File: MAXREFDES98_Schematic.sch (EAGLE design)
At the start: 34 parts, among them U1 MB110S-TP, U2 MB110S-TP, U3 MAX5969AETB+

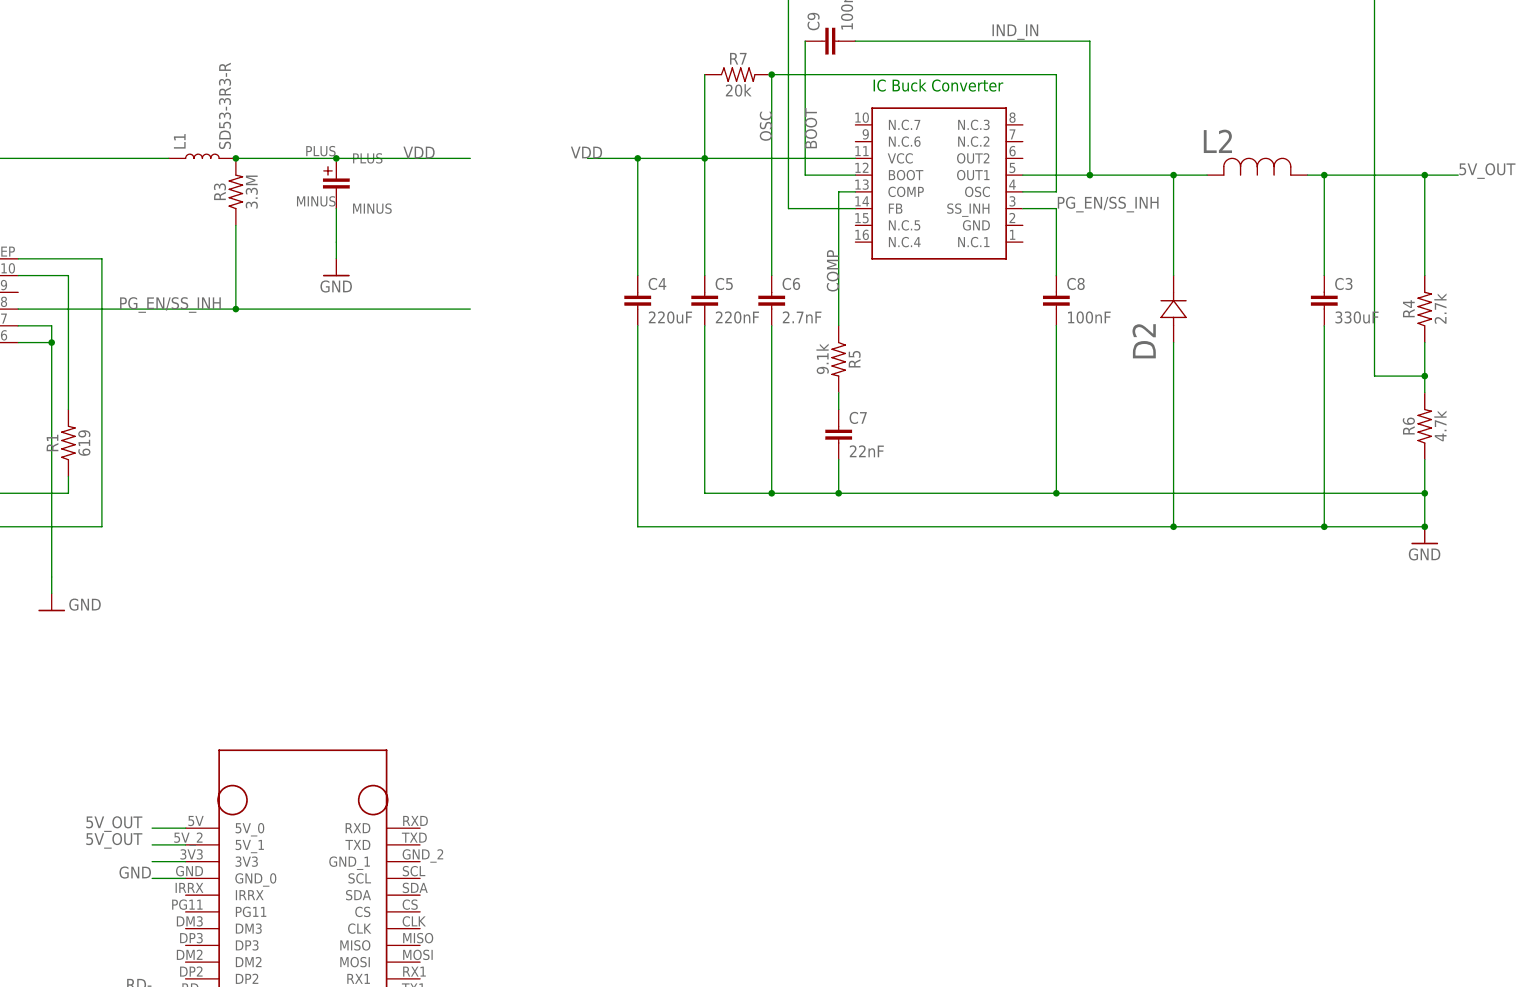
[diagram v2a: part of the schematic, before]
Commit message: Schematic fixes, parts update, replace parts on board
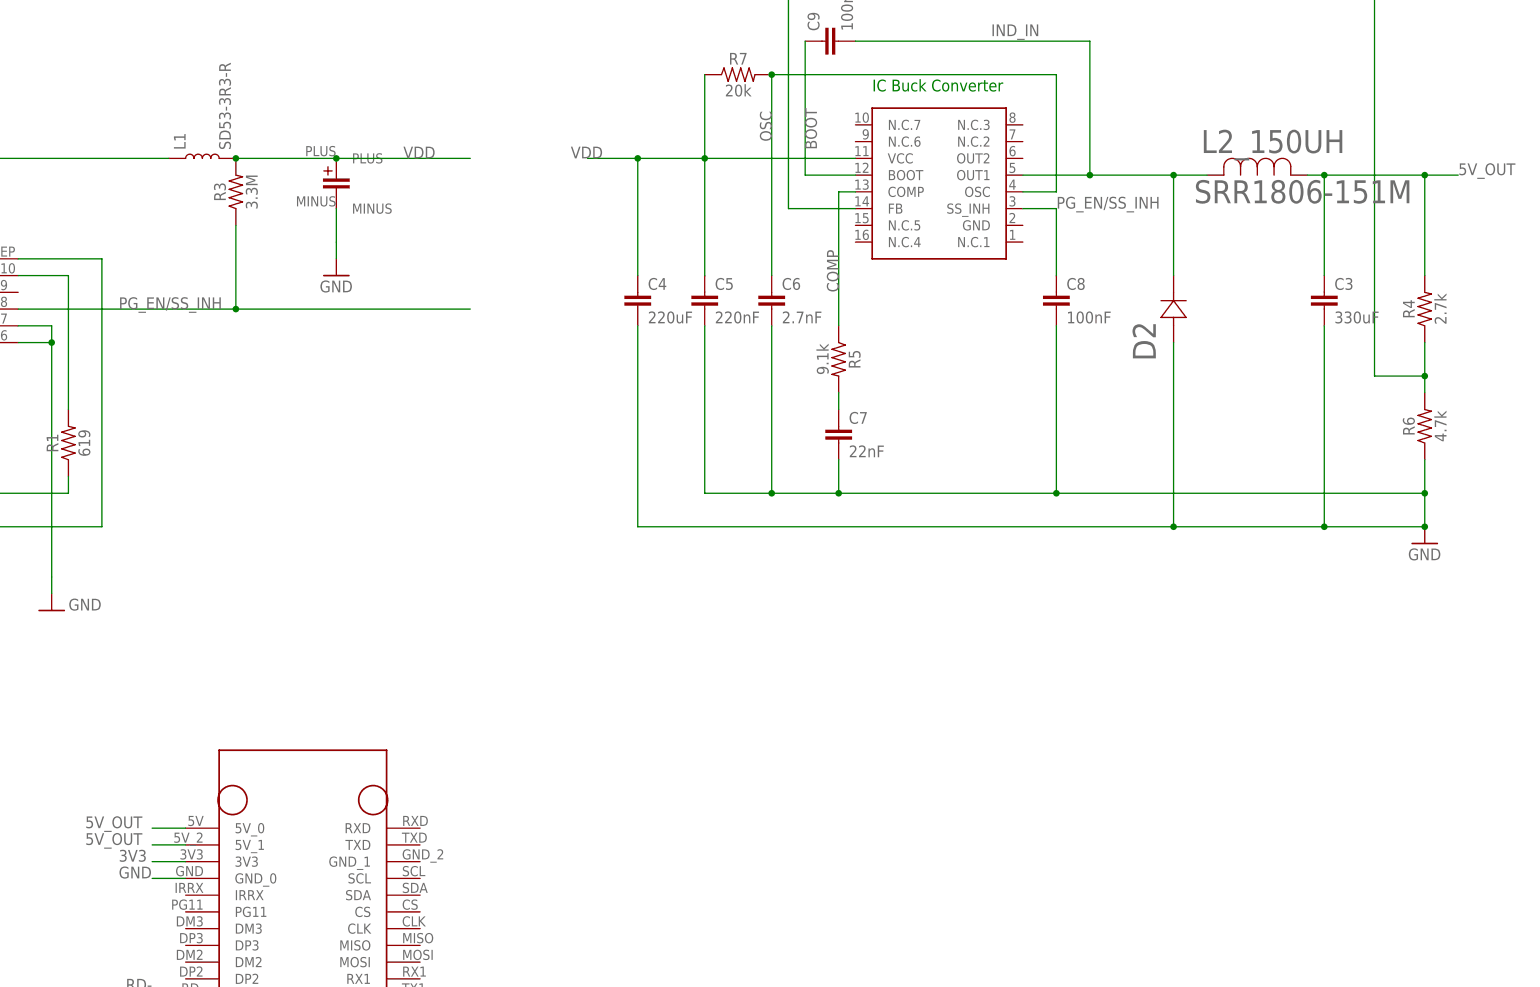
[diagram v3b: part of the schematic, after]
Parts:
- removed L2: SRR1806-151M, Camera_Board_Parts_09_30_2020:SRR1806-151M
- added L2_150UH: SRR1806-151M, CameraBoard_Library:SRR1806-151M
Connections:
- net N$8 renamed 3V3
- net 5V_OUT: now also L2_150UH.1; no longer L2.1
- net IND_IN: now also L2_150UH.2; no longer L2.2
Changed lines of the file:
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@@
 <part name="FRAME1" library="frames" library_urn="urn:adsk.eagle:library:229" deviceset="FRAME_B_L" device=""/>
 <part name="CONN" library="Camera_Board_Parts_09_30_2020" deviceset="TERM_BLOCK_PLUG_8POS_STR_2.5MM" device="" package3d_urn="urn:adsk.eagle:package:24353855/2"/>
-<part name="U$2" library="Camera_Board_Parts_09_30_2020" deviceset="NANO_PI" device=""/>
+<part name="U$2" library="Camera_Board_Parts_09_30_2020" deviceset="NANO_PI" device="" package3d_urn="urn:adsk.eagle:package:24353856/1"/>
 <part name="R10" library="SparkFun-Resistors" library_urn="urn:adsk.eagle:library:532" deviceset="0OHM" device="-0603-1/10W-5%" package3d_urn="urn:adsk.eagle:package:39650/1" value="0"/>
 <part name="R8" library="SparkFun-Resistors" library_urn="urn:adsk.eagle:library:532" deviceset="0OHM" device="-0603-1/10W-5%" package3d_urn="urn:adsk.eagle:package:39650/1" value="0"/>
@@
 <part name="GND9" library="supply1" library_urn="urn:adsk.eagle:library:371" deviceset="GND" device=""/>
 <part name="GND14" library="supply1" library_urn="urn:adsk.eagle:library:371" deviceset="GND" device=""/>
-<part name="U$1" library="Camera_Board_Parts_09_30_2020" deviceset="L4978D013TR" device=""/>
+<part name="U$1" library="Camera_Board_Parts_09_30_2020" deviceset="L4978D013TR" device="" package3d_urn="urn:adsk.eagle:package:24353853/1"/>
 <part name="C3" library="SparkFun-Capacitors" library_urn="urn:adsk.eagle:library:510" deviceset="4.7UF" device="0603" package3d_urn="urn:adsk.eagle:package:37414/1" value="330uF"/>
 <part name="C4" library="SparkFun-Capacitors" library_urn="urn:adsk.eagle:library:510" deviceset="4.7UF" device="0603" package3d_urn="urn:adsk.eagle:package:37414/1" value="220uF"/>
@@
 <part name="R7" library="SparkFun-Resistors" library_urn="urn:adsk.eagle:library:532" deviceset="0.22OHM" device="-0805-1/4W-1%" package3d_urn="urn:adsk.eagle:package:39651/1" value="20k"/>
 <part name="D2" library="Camera_Board_Parts_09_30_2020" deviceset="STPS3L60U" device="SMB_STM-M"/>
-<part name="L2" library="Camera_Board_Parts_09_30_2020" deviceset="SRR1806-151M" device=""/>
 <part name="GND2" library="supply1" library_urn="urn:adsk.eagle:library:371" deviceset="GND" device=""/>
 <part name="D3" library="SparkFun-LED" library_urn="urn:adsk.eagle:library:529" deviceset="LED" device="-FKIT-1206" package3d_urn="urn:adsk.eagle:package:39355/1"/>
@@
 <part name="R12" library="SparkFun-Resistors" library_urn="urn:adsk.eagle:library:532" deviceset="0OHM" device="-0603-1/10W-5%" package3d_urn="urn:adsk.eagle:package:39650/1" value="470"/>
 <part name="R13" library="SparkFun-Resistors" library_urn="urn:adsk.eagle:library:532" deviceset="0OHM" device="-0603-1/10W-5%" package3d_urn="urn:adsk.eagle:package:39650/1" value="470"/>
+<part name="L2_150UH" library="CameraBoard_Library" deviceset="SRR1806-151M" device=""/>
 </parts>
 <sheets>
@@
 <attribute name="NAME" x="203.0476" y="-7.8994" size="3.4798" layer="95" ratio="10" rot="SR90"/>
 </instance>
-<instance part="L2" gate="A" x="210.82" y="20.32" smashed="yes">
-<attribute name="NAME" x="209.9056" y="23.6728" size="3.4798" layer="95" ratio="10" rot="SR0"/>
-</instance>
 <instance part="GND2" gate="1" x="243.84" y="-35.56" smashed="yes">
 <attribute name="VALUE" x="241.3" y="-38.1" size="1.778" layer="96"/>
@@
 <attribute name="NAME" x="18.796" y="-71.12" size="1.778" layer="95" font="vector" rot="R90" align="bottom-center"/>
 <attribute name="VALUE" x="21.844" y="-71.12" size="1.778" layer="96" font="vector" rot="R90" align="top-center"/>
+</instance>
+<instance part="L2_150UH" gate="A" x="210.82" y="20.32" smashed="yes">
+<attribute name="VALUE" x="208.8388" y="16.0528" size="3.4798" layer="96" ratio="10" rot="SR0"/>
+<attribute name="NAME" x="209.9056" y="23.6728" size="3.4798" layer="95" ratio="10" rot="SR0"/>
 </instance>
 </instances>
@@
 <pinref part="C3" gate="G$1" pin="1"/>
 <wire x1="228.6" y1="5.08" x2="228.6" y2="20.32" width="0.1524" layer="91"/>
-<pinref part="L2" gate="A" pin="1"/>
 <wire x1="228.6" y1="20.32" x2="226.06" y2="20.32" width="0.1524" layer="91"/>
 <wire x1="228.6" y1="20.32" x2="243.84" y2="20.32" width="0.1524" layer="91"/>
@@
 <junction x="243.84" y="20.32"/>
 <label x="248.92" y="20.32" size="1.778" layer="95"/>
+<pinref part="L2_150UH" gate="A" pin="1"/>
 </segment>
 </net>
@@
 </segment>
 </net>
-<net name="N$8" class="0">
+<net name="3V3" class="0">
 <segment>
 <pinref part="U$2" gate="G$1" pin="3V3"/>
 <wire x1="55.88" y1="-83.82" x2="50.8" y2="-83.82" width="0.1524" layer="91"/>
+<label x="45.72" y="-83.82" size="1.778" layer="95"/>
 </segment>
 </net>
@@
 <pinref part="D2" gate="A" pin="1"/>
 <wire x1="205.74" y1="20.32" x2="205.74" y2="5.08" width="0.1524" layer="91"/>
-<pinref part="L2" gate="A" pin="2"/>
 <wire x1="210.82" y1="20.32" x2="205.74" y2="20.32" width="0.1524" layer="91"/>
 <junction x="205.74" y="20.32"/>
 <label x="185.42" y="43.18" size="1.778" layer="95" rot="R180"/>
-</segment>
-</net>
+<pinref part="L2_150UH" gate="A" pin="2"/>
+</segment>
+</net>

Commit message: Added clean version of Nano Pi footprint
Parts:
- U$2: value NANO_PI -> NANO_PI_CLEAN; device Camera_Board_Parts_09_30_2020:NANO_PI -> CameraBoard_Library:NANO_PI_CLEAN
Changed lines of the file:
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@@
 <part name="FRAME1" library="frames" library_urn="urn:adsk.eagle:library:229" deviceset="FRAME_B_L" device=""/>
 <part name="CONN" library="Camera_Board_Parts_09_30_2020" deviceset="TERM_BLOCK_PLUG_8POS_STR_2.5MM" device="" package3d_urn="urn:adsk.eagle:package:24353855/2"/>
-<part name="U$2" library="Camera_Board_Parts_09_30_2020" deviceset="NANO_PI" device="" package3d_urn="urn:adsk.eagle:package:24353856/1"/>
 <part name="R10" library="SparkFun-Resistors" library_urn="urn:adsk.eagle:library:532" deviceset="0OHM" device="-0603-1/10W-5%" package3d_urn="urn:adsk.eagle:package:39650/1" value="0"/>
 <part name="R8" library="SparkFun-Resistors" library_urn="urn:adsk.eagle:library:532" deviceset="0OHM" device="-0603-1/10W-5%" package3d_urn="urn:adsk.eagle:package:39650/1" value="0"/>
@@
 <part name="R13" library="SparkFun-Resistors" library_urn="urn:adsk.eagle:library:532" deviceset="0OHM" device="-0603-1/10W-5%" package3d_urn="urn:adsk.eagle:package:39650/1" value="470"/>
 <part name="L2_150UH" library="CameraBoard_Library" deviceset="SRR1806-151M" device=""/>
+<part name="U$2" library="CameraBoard_Library" deviceset="NANO_PI_CLEAN" device=""/>
 </parts>
 <sheets>
@@
 <attribute name="NAME" x="-29.591" y="-89.916" size="1.778" layer="95" rot="R90"/>
 </instance>
-<instance part="U$2" gate="G$1" x="60.96" y="-121.92" smashed="yes"/>
 <instance part="R10" gate="G$1" x="-114.3" y="-22.86" smashed="yes" rot="R90">
 <attribute name="NAME" x="-115.824" y="-22.86" size="1.778" layer="95" font="vector" rot="R90" align="bottom-center"/>
@@
 <attribute name="NAME" x="209.9056" y="23.6728" size="3.4798" layer="95" ratio="10" rot="SR0"/>
 </instance>
+<instance part="U$2" gate="G$1" x="60.96" y="-121.92" smashed="yes"/>
 </instances>
 <busses>
@@
 <net name="5V_OUT" class="0">
 <segment>
-<pinref part="U$2" gate="G$1" pin="5V_0"/>
 <wire x1="55.88" y1="-78.74" x2="50.8" y2="-78.74" width="0.1524" layer="91"/>
 <label x="40.64" y="-78.74" size="1.778" layer="95"/>
-</segment>
-<segment>
-<pinref part="U$2" gate="G$1" pin="5V_1"/>
-<wire x1="55.88" y1="-81.28" x2="50.8" y2="-81.28" width="0.1524" layer="91"/>
-<label x="40.64" y="-81.28" size="1.778" layer="95"/>
+<pinref part="U$2" gate="G$1" pin="5V_0"/>
 </segment>
 <segment>
@@
 <pinref part="L2_150UH" gate="A" pin="1"/>
 </segment>
+<segment>
+<wire x1="55.88" y1="-81.28" x2="50.8" y2="-81.28" width="0.1524" layer="91"/>
+<label x="40.64" y="-81.28" size="1.778" layer="95"/>
+<pinref part="U$2" gate="G$1" pin="5V_1"/>
+</segment>
 </net>
 <net name="GND" class="0">
@@
 </segment>
 <segment>
-<pinref part="U$2" gate="G$1" pin="GND_0"/>
 <wire x1="55.88" y1="-86.36" x2="50.8" y2="-86.36" width="0.1524" layer="91"/>
 <label x="45.72" y="-86.36" size="1.778" layer="95"/>
+<pinref part="U$2" gate="G$1" pin="GND_0"/>
 </segment>
 <segment>
@@
 <net name="3V3" class="0">
 <segment>
-<pinref part="U$2" gate="G$1" pin="3V3"/>
 <wire x1="55.88" y1="-83.82" x2="50.8" y2="-83.82" width="0.1524" layer="91"/>
 <label x="45.72" y="-83.82" size="1.778" layer="95"/>
+<pinref part="U$2" gate="G$1" pin="3V3"/>
 </segment>
 </net>
@@
 <segment>
 <wire x1="55.88" y1="-106.68" x2="50.8" y2="-106.68" width="0.1524" layer="91"/>
+<label x="50.8" y="-104.14" size="1.778" layer="95" rot="R180"/>
 <pinref part="U$2" gate="G$1" pin="RD+"/>
-<label x="50.8" y="-104.14" size="1.778" layer="95" rot="R180"/>
 </segment>
 </net>
@@
 <segment>
 <wire x1="55.88" y1="-104.14" x2="50.8" y2="-104.14" width="0.1524" layer="91"/>
+<label x="50.8" y="-101.6" size="1.778" layer="95" rot="R180"/>
 <pinref part="U$2" gate="G$1" pin="RD-"/>
-<label x="50.8" y="-101.6" size="1.778" layer="95" rot="R180"/>
 </segment>
 </net>
@@
 <segment>
 <wire x1="55.88" y1="-111.76" x2="50.8" y2="-111.76" width="0.1524" layer="91"/>
+<label x="50.8" y="-109.22" size="1.778" layer="95" rot="R180"/>
 <pinref part="U$2" gate="G$1" pin="TD+"/>
-<label x="50.8" y="-109.22" size="1.778" layer="95" rot="R180"/>
 </segment>
 </net>
@@
 <segment>
 <wire x1="55.88" y1="-109.22" x2="50.8" y2="-109.22" width="0.1524" layer="91"/>
+<label x="50.8" y="-106.68" size="1.778" layer="95" rot="R180"/>
 <pinref part="U$2" gate="G$1" pin="TD-"/>
-<label x="50.8" y="-106.68" size="1.778" layer="95" rot="R180"/>
 </segment>
 </net>
@@
 <net name="LNK" class="0">
 <segment>
-<pinref part="U$2" gate="G$1" pin="LNK"/>
 <wire x1="55.88" y1="-114.3" x2="50.8" y2="-114.3" width="0.1524" layer="91"/>
 <label x="45.72" y="-114.3" size="1.778" layer="95"/>
+<pinref part="U$2" gate="G$1" pin="LNK"/>
 </segment>
 <segment>
@@
 <net name="SPD" class="0">
 <segment>
-<pinref part="U$2" gate="G$1" pin="SPD"/>
 <wire x1="55.88" y1="-116.84" x2="50.8" y2="-116.84" width="0.1524" layer="91"/>
 <label x="45.72" y="-116.84" size="1.778" layer="95"/>
-</segment>
-<segment>
+<pinref part="U$2" gate="G$1" pin="SPD"/>
+</segment>
+<segment>
